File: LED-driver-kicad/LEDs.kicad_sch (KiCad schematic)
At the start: 54 parts, among them Q1 2N7002K, Q2 2N7002K, Q3 2N7002K, U2 MIC3205YML-TR, U5 MIC3205YML-TR, U7 MIC3205YML-TR

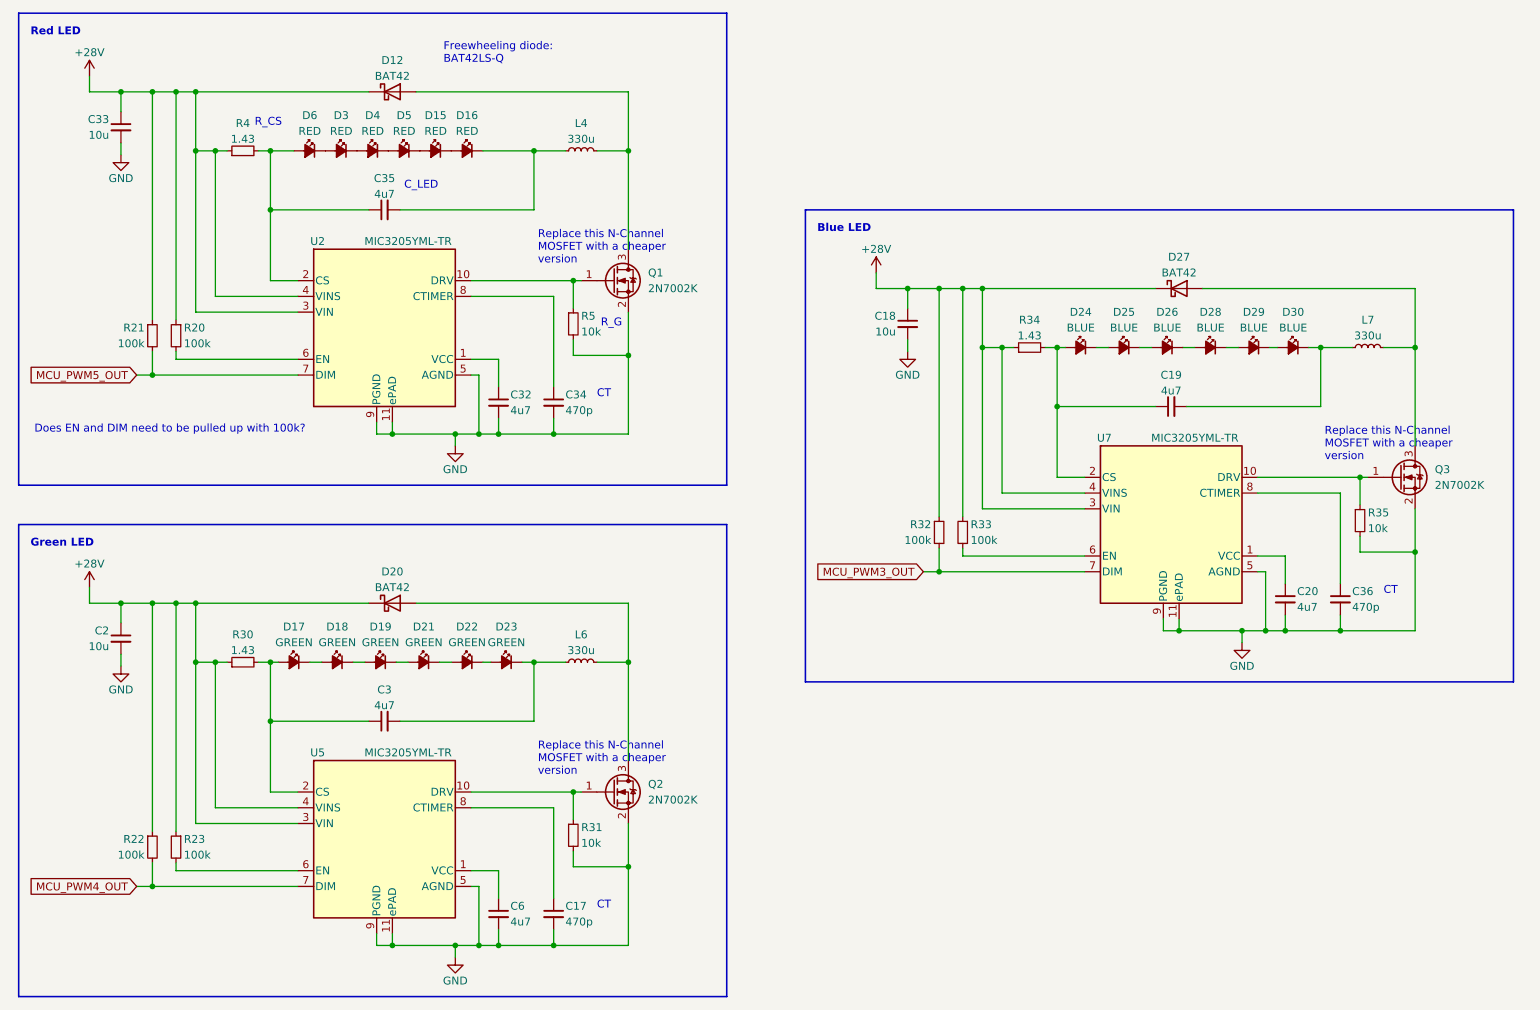
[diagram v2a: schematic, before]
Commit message: replace MOSFETs with generic n-channel MSOFETs
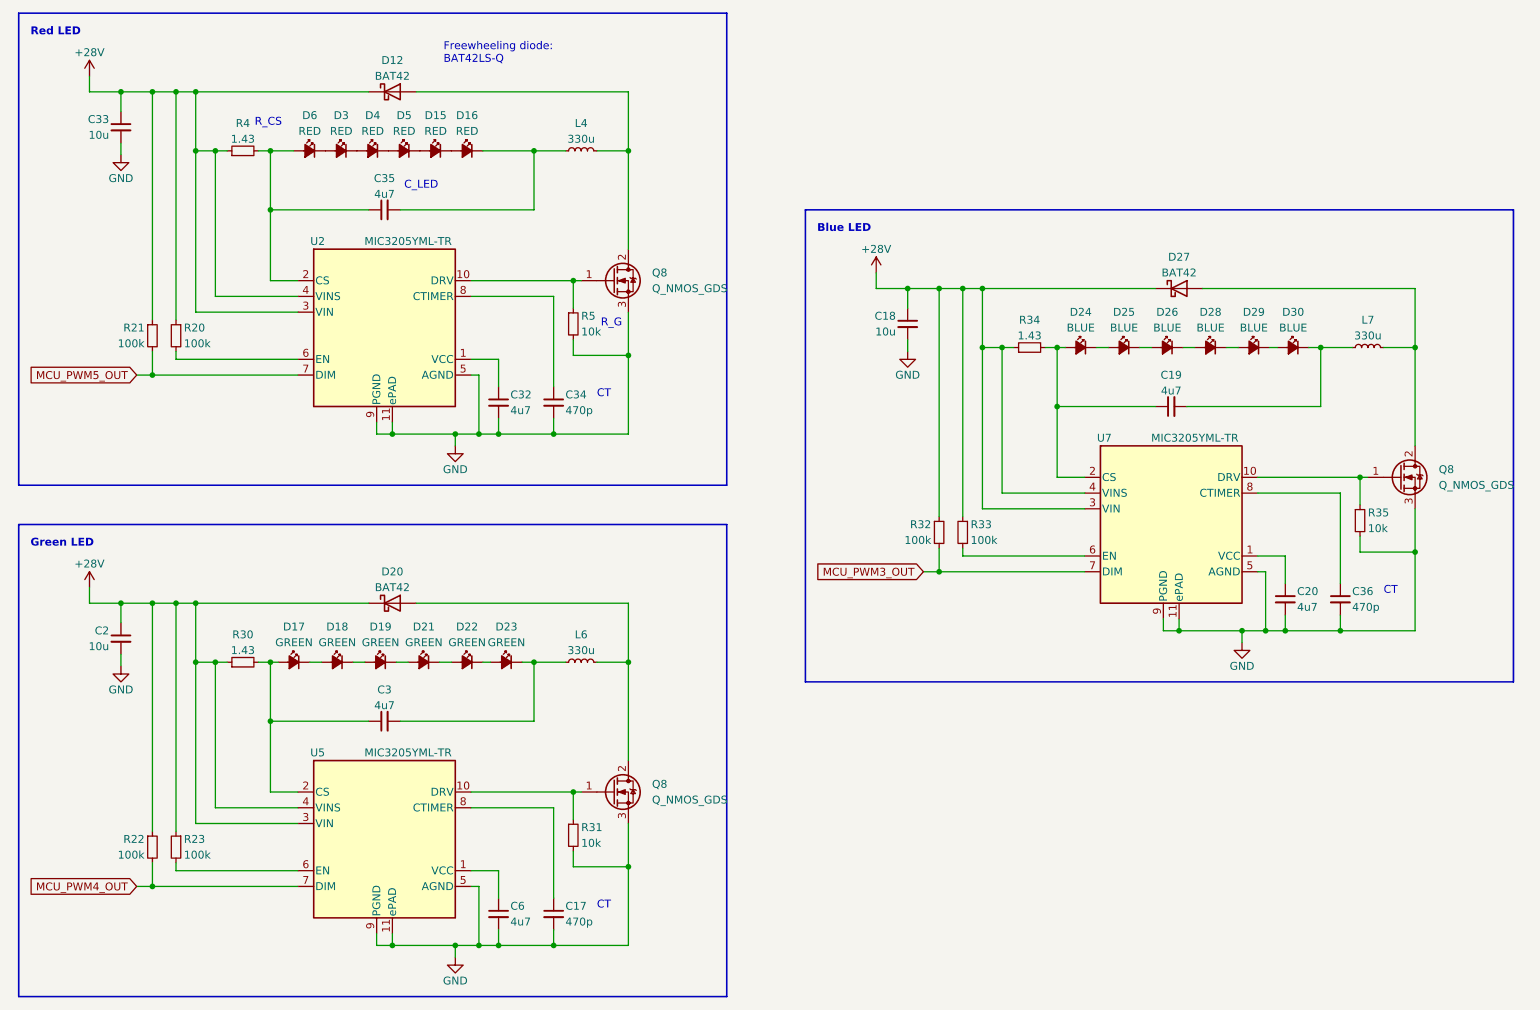
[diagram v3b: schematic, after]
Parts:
- removed Q1, Q2, Q3: 2N7002K, Package_TO_SOT_SMD:SOT-23, symbol Transistor_FET:2N7002K
- added Q8 (x3): Q_NMOS_GDS, symbol Device:Q_NMOS_GDS
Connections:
- net GND: now also Q8.3 (S), Q8.3 (S), Q8.3 (S)
- net at R5.1, U2.10 (DRV): now also Q8.1 (G)
- net at R35.1, U7.10 (DRV): now also Q8.1 (G)
- net at D27.2 (A), L7.2: now also Q8.2 (D)
- net at D12.2 (A), L4.2: now also Q8.2 (D)
- net at R31.1, U5.10 (DRV): now also Q8.1 (G)
- net at D20.2 (A), L6.2: now also Q8.2 (D)
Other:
- note removed: "Does EN and DIM need to be pulled up with 100k?"
- note removed: "Replace this N-Channel MOSFET with a cheaper version"
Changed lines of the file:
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@@
     (fill (type none))
-  )
-  (text "Replace this N-Channel\nMOSFET with a cheaper\nversion"
-    (at 102.87 59.69 0)
-    (effects (font (size 1.27 1.27)) (justify left bottom))
   )
   (text "Red LED" (at 20.955 22.86 0)
@@
   (text "Blue LED" (at 147.955 54.61 0)
     (effects (font (size 1.27 1.27) (thickness 0.254) bold) (justify left bottom))
-  )
-  (text "Replace this N-Channel\nMOSFET with a cheaper\nversion"
-    (at 102.87 142.24 0)
-    (effects (font (size 1.27 1.27)) (justify left bottom))
-  )
-  (text "Replace this N-Channel\nMOSFET with a cheaper\nversion"
-    (at 229.87 91.44 0)
-    (effects (font (size 1.27 1.27)) (justify left bottom))
-  )
-  (text "Does EN and DIM need to be pulled up with 100k?" (at 21.59 86.995 0)
-    (effects (font (size 1.27 1.27)) (justify left bottom))
   )
   (text "Green LED" (at 20.955 105.41 0)
@@
     )
   )
-  (symbol (lib_id "Transistor_FET:2N7002K") (at 241.935 93.98 0) (unit 1)
-    (in_bom yes) (on_board yes) (dnp no) (fields_autoplaced)
-    (property "Reference" "Q3" (at 247.65 92.71 0)
-      (effects (font (size 1.27 1.27)) (justify left))
-    )
-    (property "Value" "2N7002K" (at 247.65 95.25 0)
-      (effects (font (size 1.27 1.27)) (justify left))
-    )
-    (property "Footprint" "Package_TO_SOT_SMD:SOT-23" (at 247.015 95.885 0)
-      (effects (font (size 1.27 1.27) italic) (justify left) hide)
-    )
-    (property "Datasheet" "https://www.diodes.com/assets/Datasheets/ds30896.pdf" (at 241.935 93.98 0)
-      (effects (font (size 1.27 1.27)) (justify left) hide)
-    )
-    (pin "1")
-    (pin "2")
-    (pin "3")
-    (instances
-      (project "LED-driver-kicad"
-        (path "/2b071084-2ab6-4896-84cc-45b211479417/250319e1-deb8-4d57-8ee9-fb5c0c792a75"
-          (reference "Q3") (unit 1)
-        )
-        (path "/2b071084-2ab6-4896-84cc-45b211479417/b9376bb1-65c2-486f-9413-68de3cd30605"
-          (reference "Q6") (unit 1)
-        )
-      )
-    )
-  )
   (symbol (lib_id "Device:LED_Small_Filled") (at 211.455 73.025 0) (mirror y) (unit 1)
     (in_bom yes) (on_board yes) (dnp no)
@@
     )
   )
-  (symbol (lib_id "Transistor_FET:2N7002K") (at 114.935 144.78 0) (unit 1)
-    (in_bom yes) (on_board yes) (dnp no) (fields_autoplaced)
-    (property "Reference" "Q2" (at 120.65 143.51 0)
-      (effects (font (size 1.27 1.27)) (justify left))
-    )
-    (property "Value" "2N7002K" (at 120.65 146.05 0)
-      (effects (font (size 1.27 1.27)) (justify left))
-    )
-    (property "Footprint" "Package_TO_SOT_SMD:SOT-23" (at 120.015 146.685 0)
-      (effects (font (size 1.27 1.27) italic) (justify left) hide)
-    )
-    (property "Datasheet" "https://www.diodes.com/assets/Datasheets/ds30896.pdf" (at 114.935 144.78 0)
-      (effects (font (size 1.27 1.27)) (justify left) hide)
-    )
-    (pin "1")
-    (pin "2")
-    (pin "3")
-    (instances
-      (project "LED-driver-kicad"
-        (path "/2b071084-2ab6-4896-84cc-45b211479417/250319e1-deb8-4d57-8ee9-fb5c0c792a75"
-          (reference "Q2") (unit 1)
-        )
-        (path "/2b071084-2ab6-4896-84cc-45b211479417/b9376bb1-65c2-486f-9413-68de3cd30605"
-          (reference "Q5") (unit 1)
-        )
-      )
-    )
-  )
   (symbol (lib_id "Device:R_Small") (at 167.64 102.87 0) (unit 1)
     (in_bom yes) (on_board yes) (dnp no)
@@
     )
   )
+  (symbol (lib_id "Device:Q_NMOS_GDS") (at 114.935 144.78 0) (unit 1)
+    (in_bom yes) (on_board yes) (dnp no) (fields_autoplaced)
+    (property "Reference" "Q8" (at 121.285 143.51 0)
+      (effects (font (size 1.27 1.27)) (justify left))
+    )
+    (property "Value" "Q_NMOS_GDS" (at 121.285 146.05 0)
+      (effects (font (size 1.27 1.27)) (justify left))
+    )
+    (property "Footprint" "" (at 120.015 142.24 0)
+      (effects (font (size 1.27 1.27)) hide)
+    )
+    (property "Datasheet" "~" (at 114.935 144.78 0)
+      (effects (font (size 1.27 1.27)) hide)
+    )
+    (pin "1")
+    (pin "2")
+    (pin "3")
+    (instances
+      (project "LED-driver-kicad"
+        (path "/2b071084-2ab6-4896-84cc-45b211479417/b9376bb1-65c2-486f-9413-68de3cd30605"
+          (reference "Q8") (unit 1)
+        )
+        (path "/2b071084-2ab6-4896-84cc-45b211479417/250319e1-deb8-4d57-8ee9-fb5c0c792a75"
+          (reference "Q1") (unit 1)
+        )
+      )
+    )
+  )
   (symbol (lib_id "Device:C_Small") (at 232.41 113.665 0) (unit 1)
     (in_bom yes) (on_board yes) (dnp no)
@@
         (path "/2b071084-2ab6-4896-84cc-45b211479417/b9376bb1-65c2-486f-9413-68de3cd30605"
           (reference "D39") (unit 1)
-        )
-      )
-    )
-  )
-  (symbol (lib_id "Transistor_FET:2N7002K") (at 114.935 62.23 0) (unit 1)
-    (in_bom yes) (on_board yes) (dnp no) (fields_autoplaced)
-    (property "Reference" "Q1" (at 120.65 60.96 0)
-      (effects (font (size 1.27 1.27)) (justify left))
-    )
-    (property "Value" "2N7002K" (at 120.65 63.5 0)
-      (effects (font (size 1.27 1.27)) (justify left))
-    )
-    (property "Footprint" "Package_TO_SOT_SMD:SOT-23" (at 120.015 64.135 0)
-      (effects (font (size 1.27 1.27) italic) (justify left) hide)
-    )
-    (property "Datasheet" "https://www.diodes.com/assets/Datasheets/ds30896.pdf" (at 114.935 62.23 0)
-      (effects (font (size 1.27 1.27)) (justify left) hide)
-    )
-    (pin "1")
-    (pin "2")
-    (pin "3")
-    (instances
-      (project "LED-driver-kicad"
-        (path "/2b071084-2ab6-4896-84cc-45b211479417/250319e1-deb8-4d57-8ee9-fb5c0c792a75"
-          (reference "Q1") (unit 1)
-        )
-        (path "/2b071084-2ab6-4896-84cc-45b211479417/b9376bb1-65c2-486f-9413-68de3cd30605"
-          (reference "Q4") (unit 1)
         )
       )
@@
         )
       )
+    )
+  )
+  (symbol (lib_id "Device:Q_NMOS_GDS") (at 241.935 93.98 0) (unit 1)
+    (in_bom yes) (on_board yes) (dnp no) (fields_autoplaced)
+    (property "Reference" "Q8" (at 248.285 92.71 0)
+      (effects (font (size 1.27 1.27)) (justify left))
+    )
+    (property "Value" "Q_NMOS_GDS" (at 248.285 95.25 0)
+      (effects (font (size 1.27 1.27)) (justify left))
+    )
+    (property "Footprint" "" (at 247.015 91.44 0)
+      (effects (font (size 1.27 1.27)) hide)
+    )
+    (property "Datasheet" "~" (at 241.935 93.98 0)
+      (effects (font (size 1.27 1.27)) hide)
+    )
+    (pin "1")
+    (pin "2")
+    (pin "3")
+    (instances
+      (project "LED-driver-kicad"
+        (path "/2b071084-2ab6-4896-84cc-45b211479417/b9376bb1-65c2-486f-9413-68de3cd30605"
+          (reference "Q8") (unit 1)
+        )
+        (path "/2b071084-2ab6-4896-84cc-45b211479417/250319e1-deb8-4d57-8ee9-fb5c0c792a75"
+          (reference "Q2") (unit 1)
+        )
+      )
+    )
+  )
+  (symbol (lib_id "Device:Q_NMOS_GDS") (at 114.935 62.23 0) (unit 1)
+    (in_bom yes) (on_board yes) (dnp no) (fields_autoplaced)
+    (property "Reference" "Q8" (at 121.285 60.96 0)
+      (effects (font (size 1.27 1.27)) (justify left))
+    )
+    (property "Value" "Q_NMOS_GDS" (at 121.285 63.5 0)
+      (effects (font (size 1.27 1.27)) (justify left))
+    )
+    (property "Footprint" "" (at 120.015 59.69 0)
+      (effects (font (size 1.27 1.27)) hide)
+    )
+    (property "Datasheet" "~" (at 114.935 62.23 0)
+      (effects (font (size 1.27 1.27)) hide)
+    )
+    (pin "1")
+    (pin "2")
+    (pin "3")
+    (instances
+      (project "LED-driver-kicad"
+        (path "/2b071084-2ab6-4896-84cc-45b211479417/b9376bb1-65c2-486f-9413-68de3cd30605"
+          (reference "Q8") (unit 1)
+        )
+        (path "/2b071084-2ab6-4896-84cc-45b211479417/250319e1-deb8-4d57-8ee9-fb5c0c792a75"
+          (reference "Q6") (unit 1)
+        )
+      )

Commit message: update comments and title blocks
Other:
- title: (none) -> Photogrammetry Rig - LED Driver
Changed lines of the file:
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@@
 (kicad_sch (version 20230121) (generator eeschema)
   (paper "A4")
+  (title_block
+    (title "Photogrammetry Rig - LED Driver")
+    (date "2023-08-02")
+    (rev "0.1.0")
+  )
   (junction (at 59.69 133.35) (diameter 0) (color 0 0 0 0)
   )

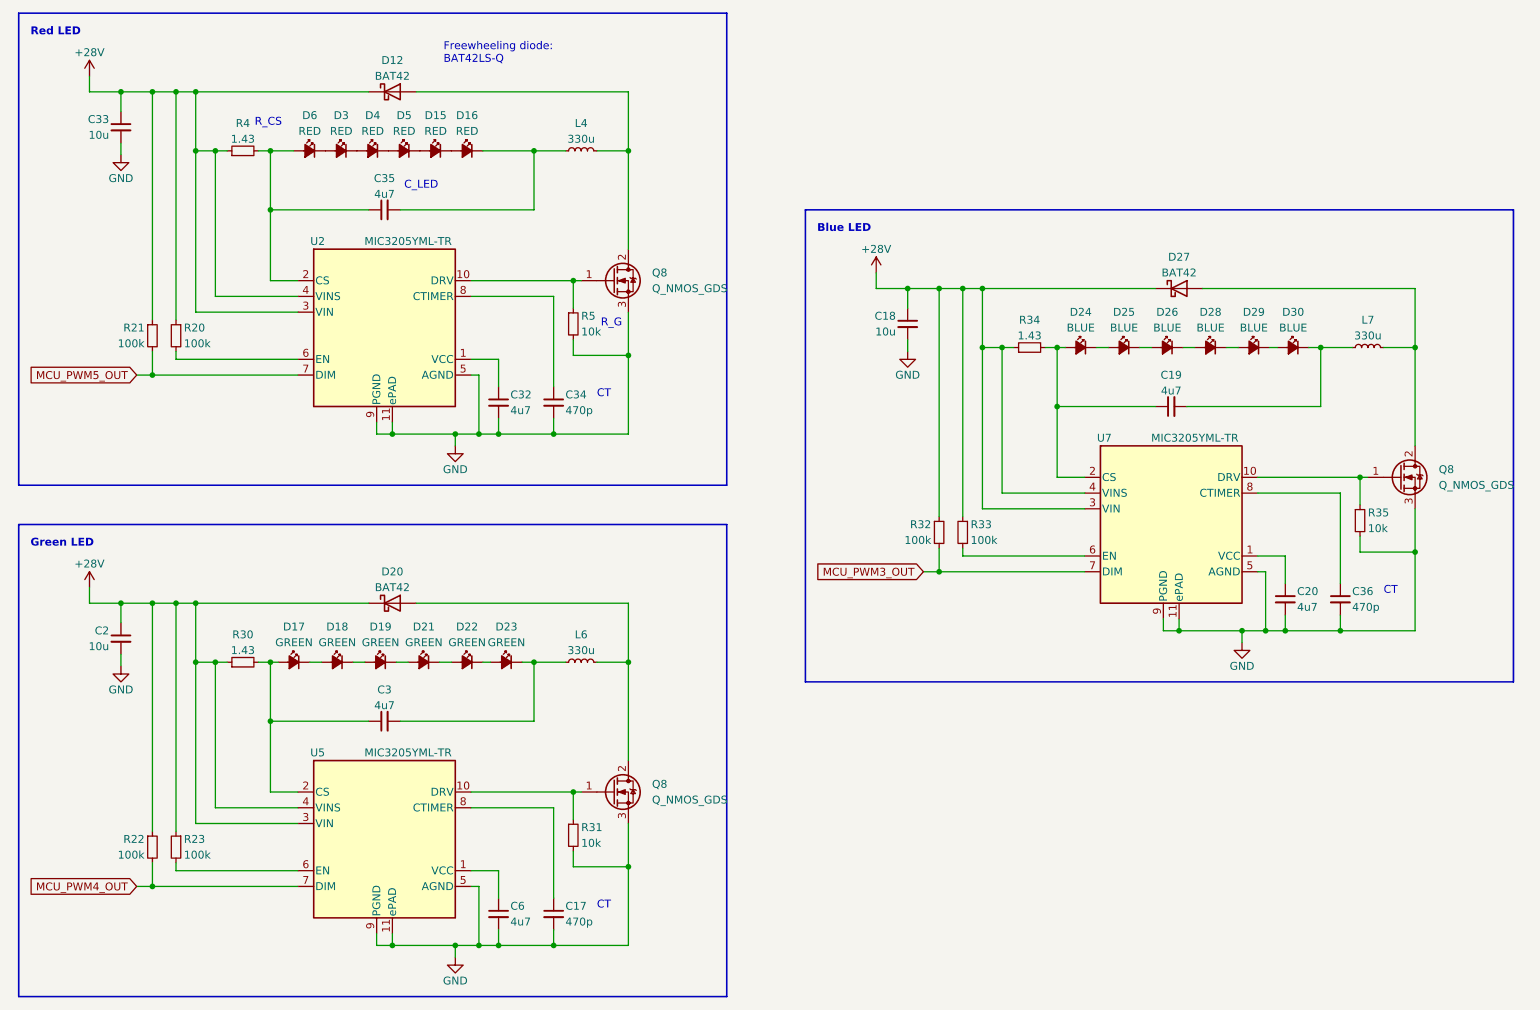
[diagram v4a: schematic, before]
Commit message: update component designators
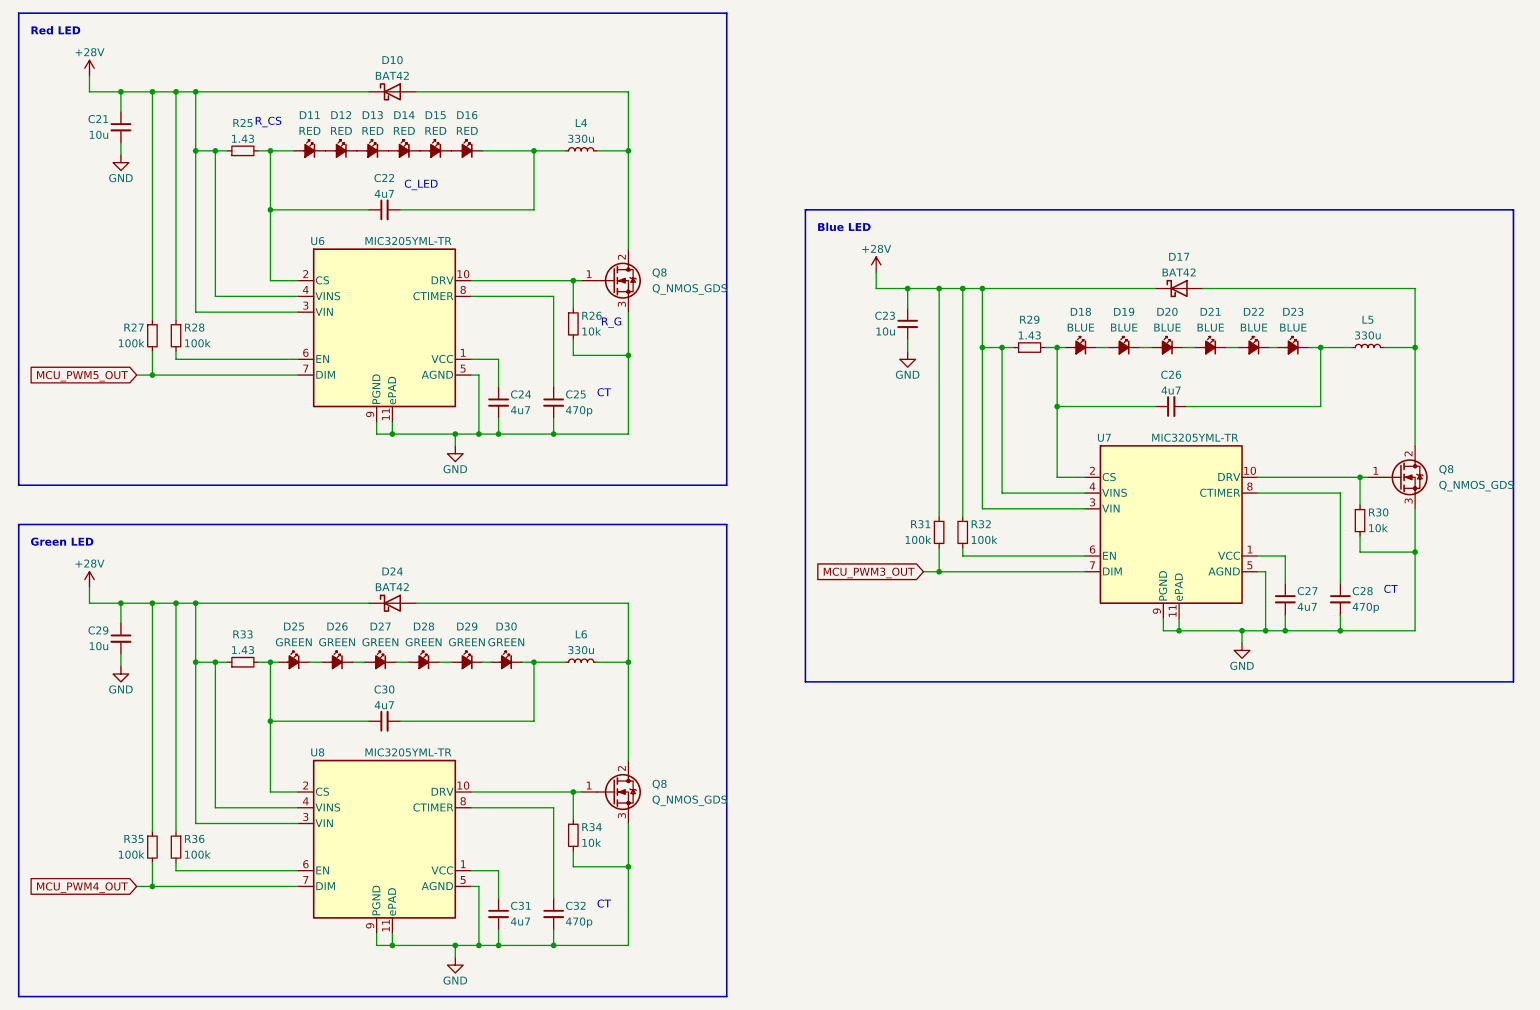
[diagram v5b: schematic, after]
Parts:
- renumbered C33 to C21, C35 to C22, C18 to C23, C32 to C24, C34 to C25, C19 to C26, C20 to C27, C36 to C28, C2 to C29, C3 to C30, C6 to C31, C17 to C32, D12 to D10, D6 to D11, D3 to D12, D4 to D13, D5 to D14, D27 to D17, D24 to D18, D25 to D19, D26 to D20, D28 to D21, D29 to D22, D30 to D23, D20 to D24, D17 to D25, D18 to D26, D19 to D27, D21 to D28, D22 to D29, D23 to D30, L7 to L5, R4 to R25, R5 to R26, R21 to R27, R20 to R28, R34 to R29, R35 to R30, R32 to R31, R33 to R32, R30 to R33, R31 to R34, R22 to R35, R23 to R36, U2 to U6, U5 to U8
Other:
- note removed: "Freewheeling diode: BAT42LS-Q"

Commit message: update footprint assignments
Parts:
- C21, C23, C29: footprint (none) -> Capacitor_SMD:C_1206_3216Metric
- C22, C24, C26, C27, C30, C31: footprint (none) -> Capacitor_SMD:C_0805_2012Metric
- C25, C28, C32: footprint (none) -> Capacitor_SMD:C_0402_1005Metric
- D11, D12, D13, D14, D15, D16, D18, D19, D20, D21, D22, D23, D25, D26, D27, D28, D29, D30: footprint (none) -> LED_SMD:LED_Cree-JE2835_3V_NClass
- L4, L5, L6: footprint (none) -> Inductor_SMD:L_1812_4532Metric
- R25, R26, R27, R28, R29, R30, R31, R32, R33, R34, R35, R36: footprint (none) -> Resistor_SMD:R_0402_1005Metric
- U6: footprint Mahabeer-Package_DFN_QFN:MLF-10_ML_MCH-Driver_LED_Microchip_MIC3205YML-TR -> KM-Package_DFN_QFN:MLF-10_ML_MCH-Driver_LED_Microchip_MIC3205YML-TR
